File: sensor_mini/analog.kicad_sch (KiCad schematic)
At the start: 41 parts, among them J2 Conn_01x02_Female-Connector, J3 Conn_01x02_Female-Connector, J4 Conn_01x02_Female-Connector, J5 Conn_01x02_Female-Connector, U4 TLV9002IDR

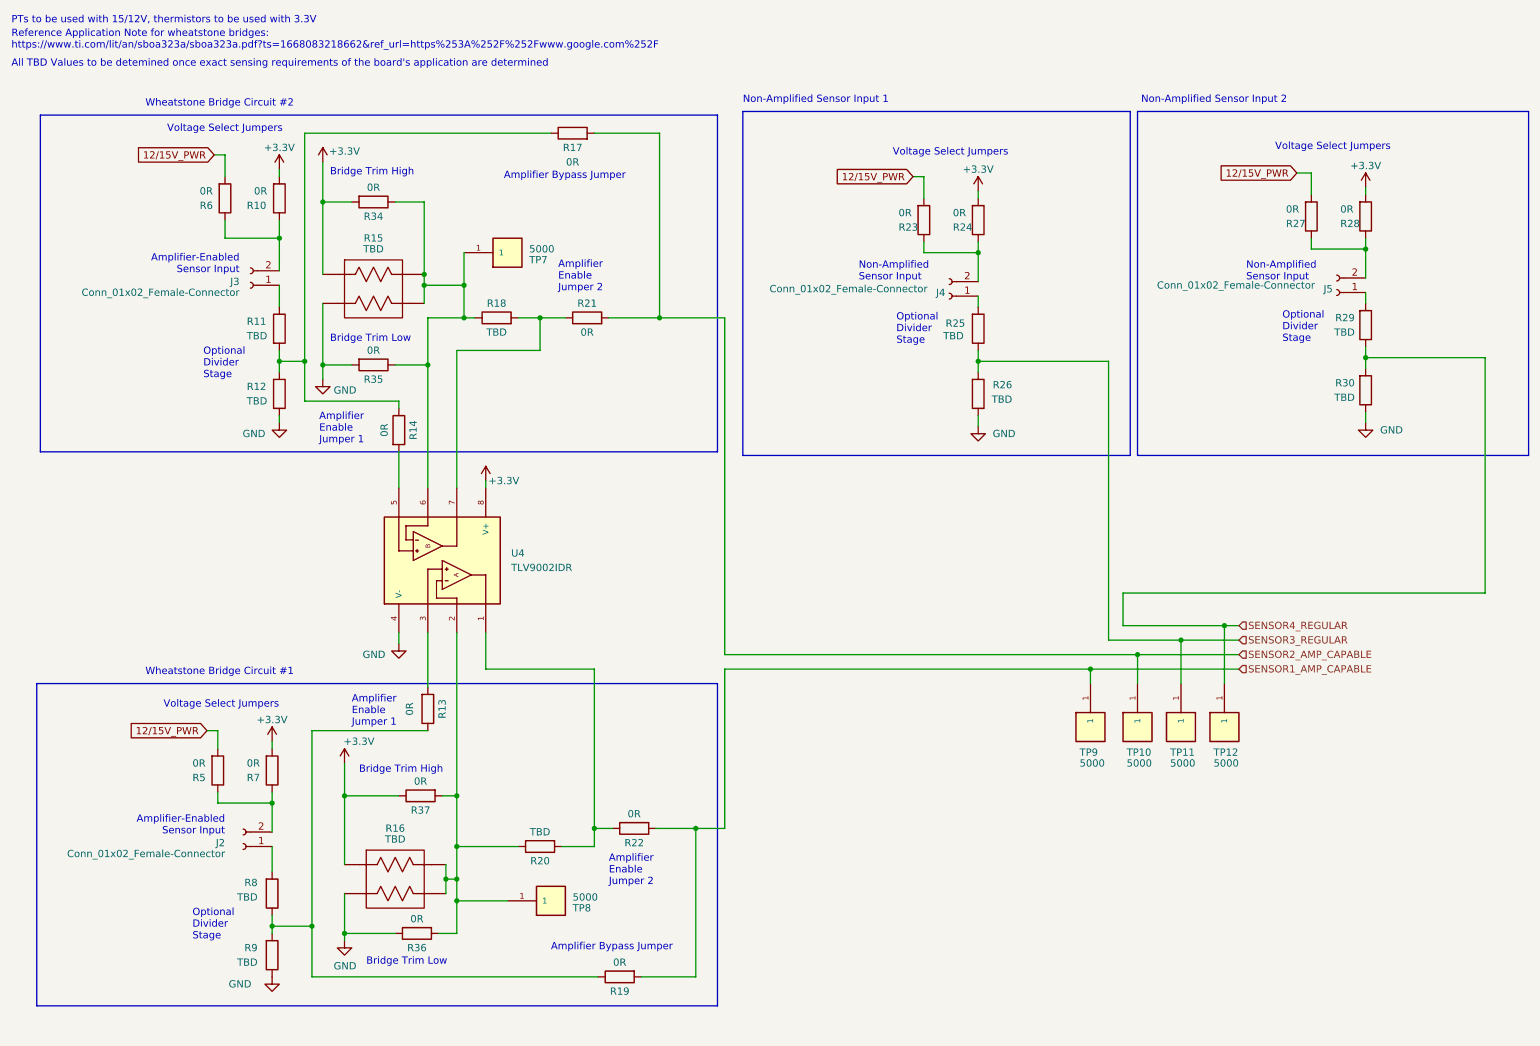
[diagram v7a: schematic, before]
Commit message: Begin addressing PR comments
Added values, replaced 5->3.3regulator, added decoupling caps, fixed barometer address, accommodated 3-pin connectors, added LEDs, addedd interrupt pin, changed inductor formatting
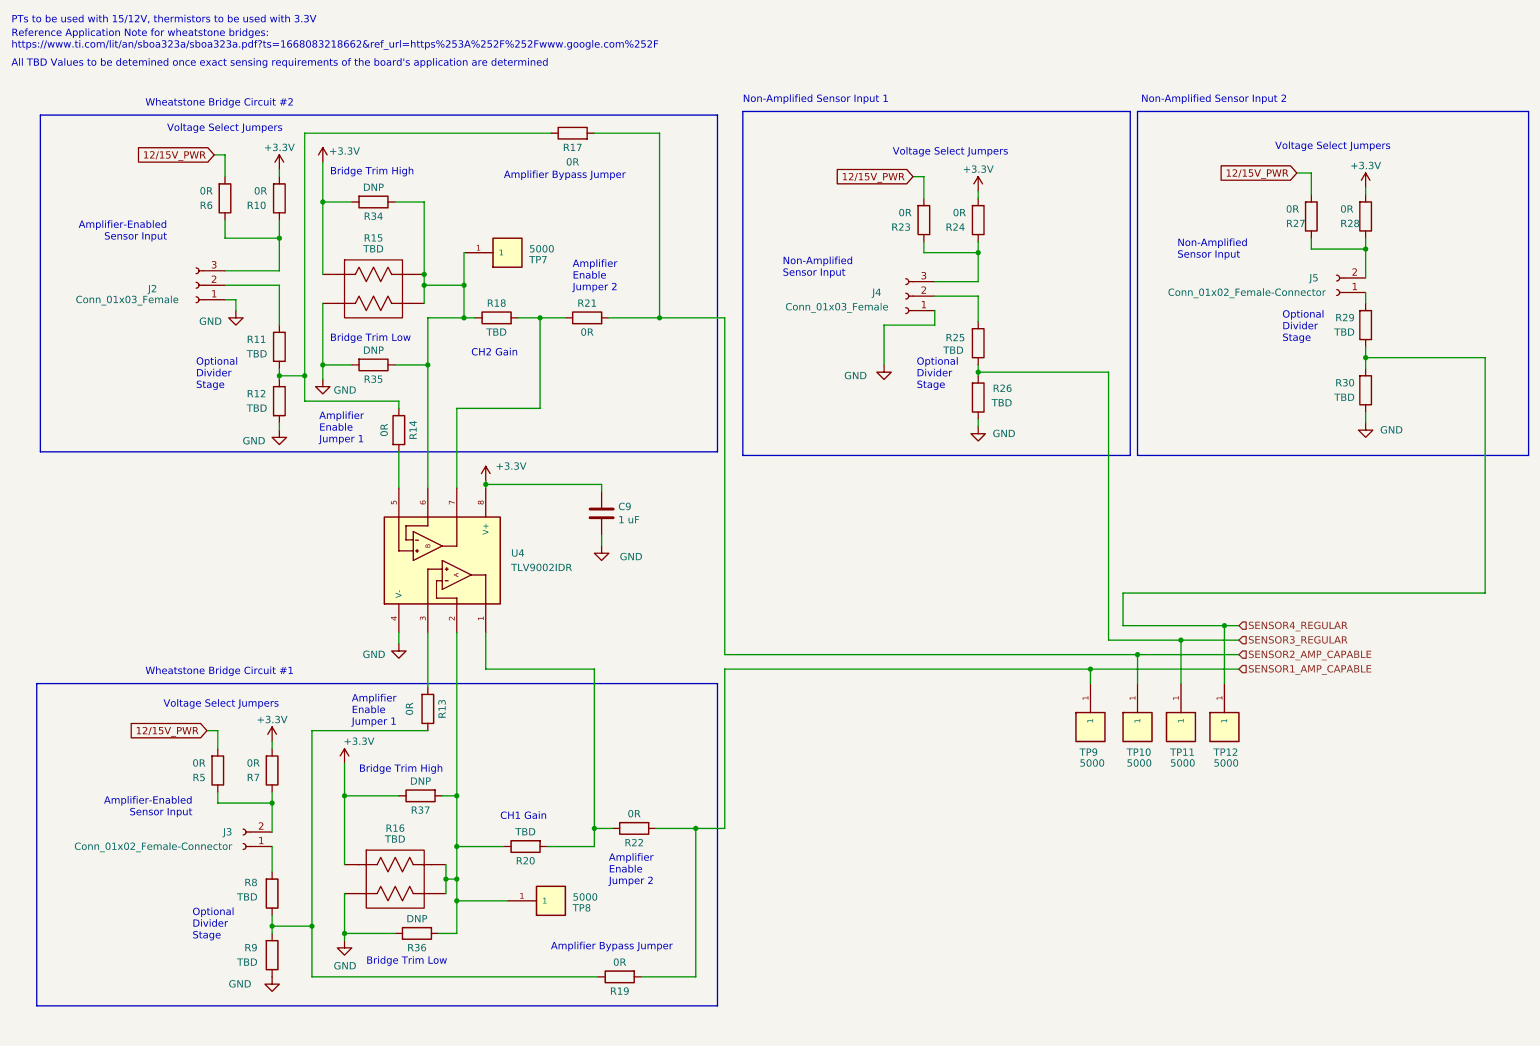
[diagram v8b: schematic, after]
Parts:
- removed J2, J4: Conn_01x02_Female-Connector, Connector_JST:JST_PH_S2B-PH-K_1x02_P2.00mm_Horizontal, symbol Connector:Conn_01x02_Female
- added C9: 1 uF, Capacitor_SMD:C_0805_2012Metric_Pad1.15x1.40mm_HandSolder, symbol Device:C
- added J2, J4: Conn_01x03_Female, symbol Connector:Conn_01x03_Female
- R34, R35, R36, R37: value 0R -> DNP
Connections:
- net +3V3: now also C9.1
- net GND: now also C9.2, J2.1 (Pin_1), J4.1 (Pin_1)
- net at R8.2: now also J3.1 (Pin_1)
- net at R5.1, R7.1: now also J3.2 (Pin_2)
- net at R10.1, R6.1: now also J2.3 (Pin_3); no longer J3.2 (Pin_2)
- net at R11.1: now also J2.2 (Pin_2); no longer J3.1 (Pin_1)
- net at R23.1, R24.1: now also J4.3 (Pin_3)
- net at R25.2: now also J4.2 (Pin_2)
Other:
- note added: "CH1 Gain"
- note added: "CH2 Gain"
- moved on the sheet: R11, R12, R20, R25, R26
